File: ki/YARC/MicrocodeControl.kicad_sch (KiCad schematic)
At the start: 24 parts, among them U31 74LS32, U44 74LS574, U45 74LS574, U46 74LS157, U47 74LS157, U48 74LS193, U49 74LS193, U50 74LS139, U51 74LS32, U52 74LS32, U53 74LS157, U54 74LS32

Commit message: Cleanups on the way to first execution - no significant functional changes
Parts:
- renumbered U31 to U54, U44 to U55, U45 to U56, U46 to U57, U47 to U58, U48 to U59, U49 to U60, U50 to U61, U51 to U62, U52 to U63, U53 to U64, U54 to U65
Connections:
- net ~{UC_RAM_OE}: no longer names the net of U60.6 (QC)

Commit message: Add delay line for general register write signal. Minor corrections and cleanups.
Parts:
- renumbered U54 to U31, U55 to U44, U56 to U45, U57 to U46, U58 to U47, U59 to U48, U60 to U49, U61 to U50, U62 to U51, U63 to U52, U64 to U53, U65 to U54

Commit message: Convert schematic to KiCad 7
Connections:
- net GND: now also U54.7 (GND)
- net KCLK0: now also U52.6, U54.11, U54.8; no longer U52.3, U54.3, U54.3
- net SYSCLK: now also U51.4, U51.9, U52.12, U52.4, U54.12, U54.9; no longer U51.1, U51.1, U52.1, U52.1, U54.1, U54.1
- net VCC: now also U54.14 (VCC)
- net ~{KI0EN}: now also U52.10; no longer U52.2
- net ~{KI1EN}: now also U51.13, U51.6; no longer U51.2, U51.3
- net ~{KI2EN}: now also U31.4, U51.8; no longer U31.1, U51.3
- net ~{KI3EN}: now also U52.11; no longer U52.3
- net ~{UC_WE0}: now also U52.8; no longer U52.3
- net ~{UC_WE1}: now also U51.11; no longer U51.3
- net ~{UC_WE2}: now also U31.6; no longer U31.3
- net at U53.9 (Zc): now also U54.10; no longer U54.2
- net at U50.7 (~{Q3}): now also U52.13; no longer U52.2
- net at U53.12 (Zd): now also U54.13; no longer U54.2
- net at U53.11 (I0c): now also U50.10 (~{Q2}); no longer U50.6 (~{Q2})
- net at U53.14 (I0d): now also U50.9 (~{Q3}); no longer U50.7 (~{Q3})
- net at U53.2 (I0a): now also U50.12 (~{Q0}); no longer U50.4 (~{Q0})
- net at U53.5 (I0b): now also U50.11 (~{Q1}); no longer U50.5 (~{Q1})
- net at U53.7 (Zb): now also U52.5; no longer U52.2
- net at U45.13 (Q6): now also U50.15 (~{EN}); no longer U50.1 (~{EN})
- net at U45.14 (Q5): now also U50.13 (B); no longer U50.3 (B)
- net at U45.15 (Q4): now also U50.14 (A); no longer U50.2 (A)
- net at U50.6 (~{Q2}): now also U51.10; no longer U51.2
- net at U50.5 (~{Q1}): now also U51.5; no longer U51.2
- new net: U31.5, U45.16 (Q3), U51.12, U51.2, U52.9

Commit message: Removed about 2/3 of 2300+ errors from the ERC
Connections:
- net KCLK0: no longer U52.6, U54.11, U54.8
- new net KCLK1: U52.6
- new net KCLK2: U54.8
- new net KCLK3: U54.11

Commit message: Ongoing fixes for ERC errors
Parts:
- removed U44: 74LS574, symbol 74xx:74LS574
- renumbered U31 to U54, U45 to U56, U46 to U57, U47 to U58, U48 to U59, U49 to U60, U50 to U61, U51 to U62, U52 to U63, U53 to U64, U54 to U65
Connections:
- net GND: now also U60.14 (CLR), U62.7 (GND), U63.7 (GND)
- net VCC: now also U62.14 (VCC), U63.14 (VCC)
- no-connect marks 0 -> 6
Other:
- note removed: "ALSO ON SHT 8"
- note removed: "IR HIGH (IRH)"

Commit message: Continuing cleanup of schematic
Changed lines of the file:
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@@
     (stroke (width 0) (type default))
   )
-  (bus (pts (xy 60.96 152.4) (xy 60.96 161.29))
+  (bus (pts (xy 60.96 134.62) (xy 60.96 161.29))
     (stroke (width 0) (type default))
   )
@@
     (stroke (width 0) (type default))
   )
-  (bus (pts (xy 60.96 144.78) (xy 60.96 147.32))
-    (stroke (width 0) (type default))
-  )
   (wire (pts (xy 137.16 166.37) (xy 137.16 163.83))
     (stroke (width 0) (type default))
@@
     (stroke (width 0) (type default))
   )
-  (bus (pts (xy 60.96 142.24) (xy 60.96 144.78))
-    (stroke (width 0) (type default))
-  )
   (wire (pts (xy 137.16 105.41) (xy 137.16 107.95))
     (stroke (width 0) (type default))
@@
     (stroke (width 0) (type default))
   )
-  (bus (pts (xy 60.96 139.7) (xy 60.96 142.24))
-    (stroke (width 0) (type default))
-  )
   (wire (pts (xy 105.41 161.29) (xy 111.76 161.29))
     (stroke (width 0) (type default))
@@
     (stroke (width 0) (type default))
   )
-  (bus (pts (xy 60.96 134.62) (xy 60.96 137.16))
-    (stroke (width 0) (type default))
-  )
   (wire (pts (xy 228.6 24.13) (xy 245.11 24.13))
     (stroke (width 0) (type default))
@@
     (stroke (width 0) (type default))
   )
-  (bus (pts (xy 60.96 147.32) (xy 60.96 149.86))
-    (stroke (width 0) (type default))
-  )
   (wire (pts (xy 166.37 57.15) (xy 173.99 57.15))
     (stroke (width 0) (type default))
@@
     (stroke (width 0) (type default))
   )
-  (bus (pts (xy 60.96 149.86) (xy 60.96 152.4))
-    (stroke (width 0) (type default))
-  )
   (wire (pts (xy 55.88 45.72) (xy 111.76 45.72))
     (stroke (width 0) (type default))
@@
     (stroke (width 0) (type default))
   )
-  (bus (pts (xy 60.96 137.16) (xy 60.96 139.7))
-    (stroke (width 0) (type default))
-  )

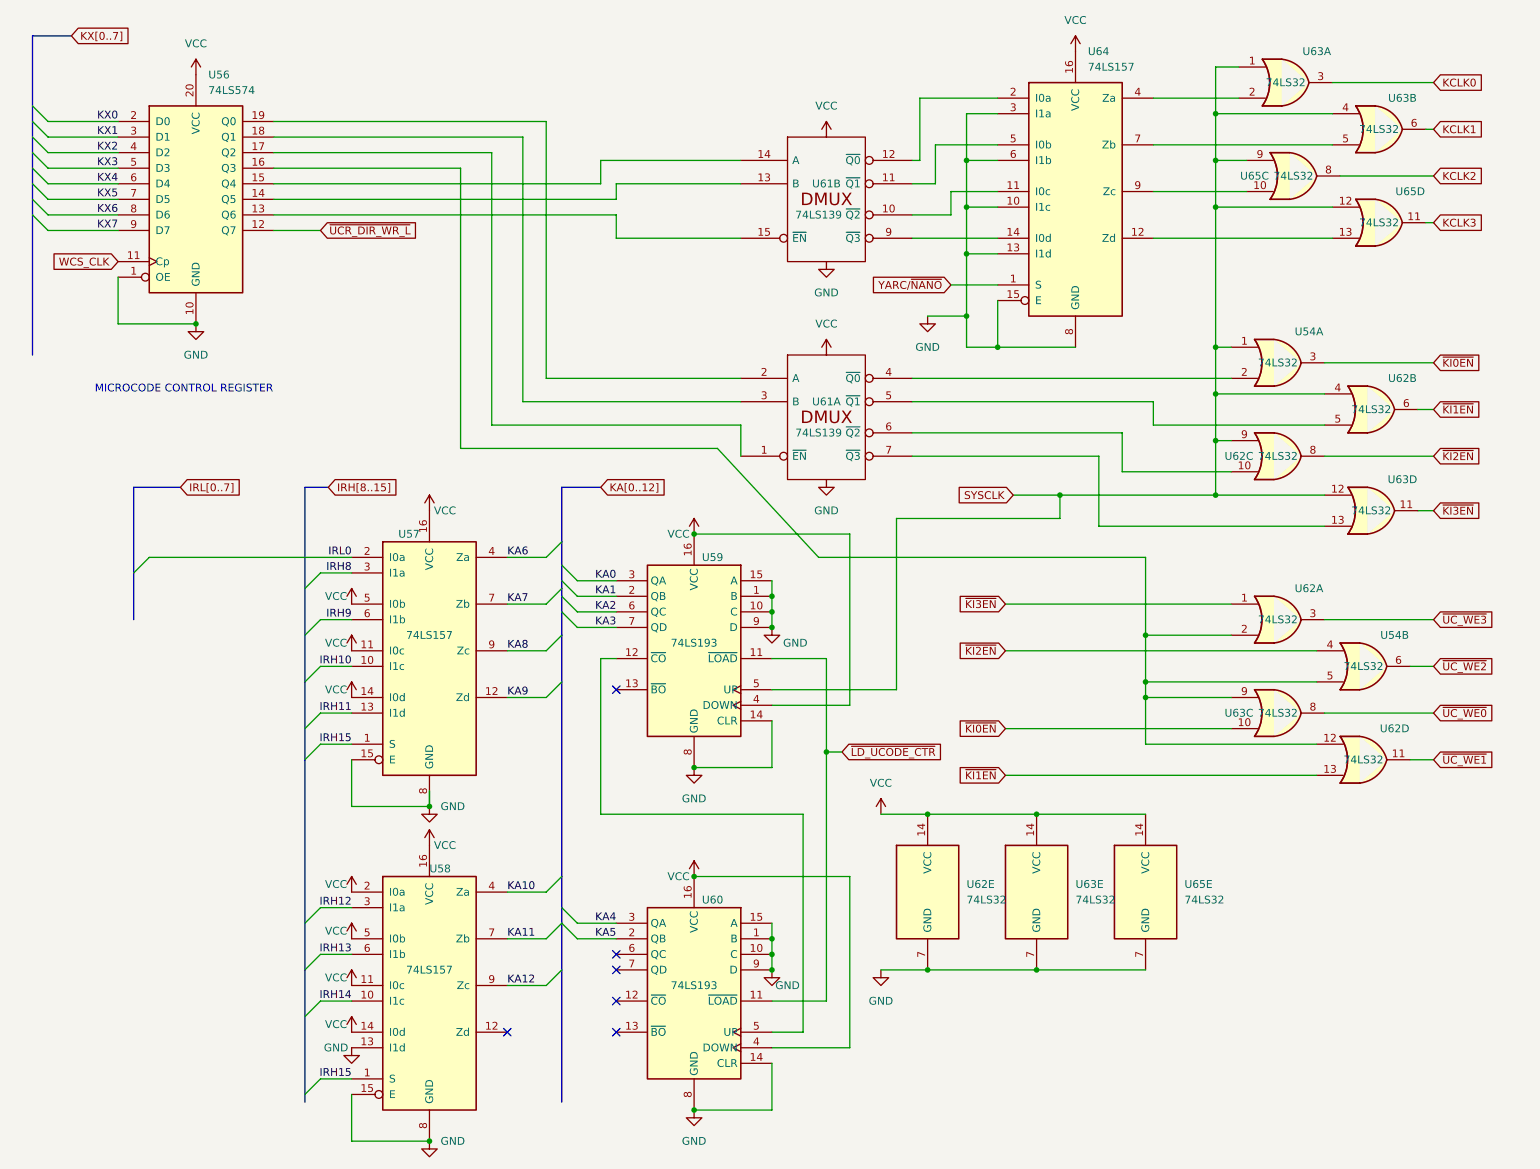
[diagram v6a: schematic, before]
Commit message: Schematic for addressing unit is complete and all ERC violations addressed
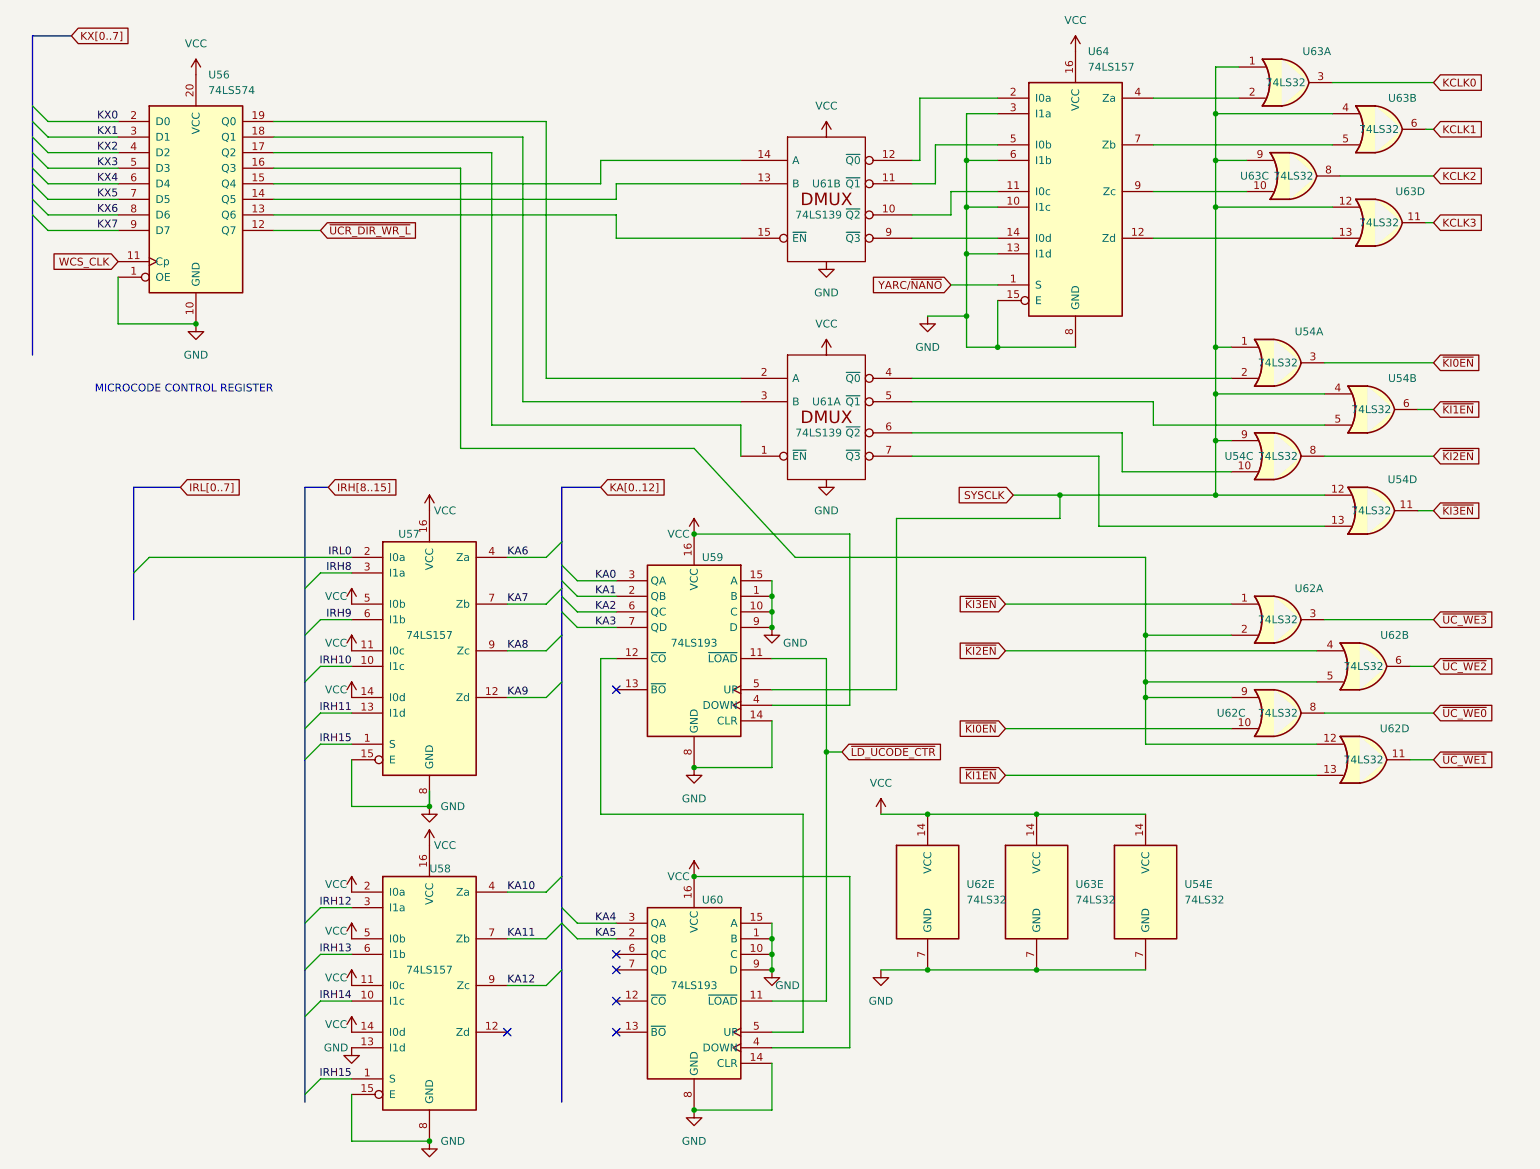
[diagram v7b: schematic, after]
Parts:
- renumbered U63 to U54, U62 to U54, U65 to U54, U54 to U62, U63 to U62, U65 to U63
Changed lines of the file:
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@@
     (stroke (width 0) (type default))
   )
-  (wire (pts (xy 86.36 83.82) (xy 128.27 83.82))
+  (wire (pts (xy 86.36 83.82) (xy 124.46 83.82))
     (stroke (width 0) (type default))
   )
@@
     (stroke (width 0) (type default))
   )
-  (wire (pts (xy 144.78 101.6) (xy 198.12 101.6))
+  (wire (pts (xy 140.97 101.6) (xy 198.12 101.6))
     (stroke (width 0) (type default))
   )
@@
     (stroke (width 0) (type default))
   )
-  (wire (pts (xy 128.27 83.82) (xy 144.78 101.6))
+  (wire (pts (xy 124.46 83.82) (xy 140.97 101.6))
     (stroke (width 0) (type default))
   )
@@
   (symbol (lib_id "74xx:74LS32") (at 222.25 39.37 0) (unit 3)
     (in_bom yes) (on_board yes) (dnp no)
-    (property "Reference" "U65" (at 215.9 39.37 0)
+    (property "Reference" "U63" (at 215.9 39.37 0)
       (effects (font (size 1.27 1.27)))
     )
@@
       (project "YARC"
         (path "/22e0f8e1-b0d7-4d47-bb7c-8ef04cd95fca/a3892bed-2422-46c3-a2f7-c55c7ea6ac93"
-          (reference "U65") (unit 3)
+          (reference "U63") (unit 3)
         )
       )
@@
   (symbol (lib_id "74xx:74LS32") (at 234.95 93.98 0) (unit 4)
     (in_bom yes) (on_board yes) (dnp no)
-    (property "Reference" "U63" (at 240.03 88.9 0)
+    (property "Reference" "U54" (at 240.03 88.9 0)
       (effects (font (size 1.27 1.27)))
     )
@@
       (project "YARC"
         (path "/22e0f8e1-b0d7-4d47-bb7c-8ef04cd95fca/a3892bed-2422-46c3-a2f7-c55c7ea6ac93"
-          (reference "U63") (unit 4)
+          (reference "U54") (unit 4)
         )
       )
@@
   (symbol (lib_id "74xx:74LS32") (at 236.22 46.99 0) (unit 4)
     (in_bom yes) (on_board yes) (dnp no)
-    (property "Reference" "U65" (at 241.3 41.91 0)
+    (property "Reference" "U63" (at 241.3 41.91 0)
       (effects (font (size 1.27 1.27)))
     )
@@
       (project "YARC"
         (path "/22e0f8e1-b0d7-4d47-bb7c-8ef04cd95fca/a3892bed-2422-46c3-a2f7-c55c7ea6ac93"
-          (reference "U65") (unit 4)
+          (reference "U63") (unit 4)
         )
       )
@@
   (symbol (lib_id "74xx:74LS32") (at 233.68 119.38 0) (unit 2)
     (in_bom yes) (on_board yes) (dnp no)
-    (property "Reference" "U54" (at 238.76 114.3 0)
+    (property "Reference" "U62" (at 238.76 114.3 0)
       (effects (font (size 1.27 1.27)))
     )
@@
       (project "YARC"
         (path "/22e0f8e1-b0d7-4d47-bb7c-8ef04cd95fca/a3892bed-2422-46c3-a2f7-c55c7ea6ac93"
-          (reference "U54") (unit 2)
+          (reference "U62") (unit 2)
         )
       )
@@
   (symbol (lib_id "74xx:74LS32") (at 219.71 85.09 0) (unit 3)
     (in_bom yes) (on_board yes) (dnp no)
-    (property "Reference" "U62" (at 213.36 85.09 0)
+    (property "Reference" "U54" (at 213.36 85.09 0)
       (effects (font (size 1.27 1.27)))
     )
@@
       (project "YARC"
         (path "/22e0f8e1-b0d7-4d47-bb7c-8ef04cd95fca/a3892bed-2422-46c3-a2f7-c55c7ea6ac93"
-          (reference "U62") (unit 3)
+          (reference "U54") (unit 3)
         )
       )
@@
   (symbol (lib_id "74xx:74LS32") (at 219.71 127 0) (unit 3)
     (in_bom yes) (on_board yes) (dnp no)
-    (property "Reference" "U63" (at 213.36 127 0)
+    (property "Reference" "U62" (at 212.09 127 0)
       (effects (font (size 1.27 1.27)))
     )
@@
       (project "YARC"
         (path "/22e0f8e1-b0d7-4d47-bb7c-8ef04cd95fca/a3892bed-2422-46c3-a2f7-c55c7ea6ac93"
-          (reference "U63") (unit 3)
+          (reference "U62") (unit 3)
         )
       )
@@
   (symbol (lib_id "74xx:74LS32") (at 234.95 77.47 0) (unit 2)
     (in_bom yes) (on_board yes) (dnp no)
-    (property "Reference" "U62" (at 240.03 72.39 0)
+    (property "Reference" "U54" (at 240.03 72.39 0)
       (effects (font (size 1.27 1.27)))
     )
@@
       (project "YARC"
         (path "/22e0f8e1-b0d7-4d47-bb7c-8ef04cd95fca/a3892bed-2422-46c3-a2f7-c55c7ea6ac93"
-          (reference "U62") (unit 2)
+          (reference "U54") (unit 2)
         )
       )
@@
   (symbol (lib_id "74xx:74LS32") (at 198.12 156.21 0) (unit 5)
     (in_bom yes) (on_board yes) (dnp no) (fields_autoplaced)
-    (property "Reference" "U65" (at 204.47 154.9399 0)
+    (property "Reference" "U54" (at 204.47 154.9399 0)
       (effects (font (size 1.27 1.27)) (justify left))
     )
@@
       (project "YARC"
         (path "/22e0f8e1-b0d7-4d47-bb7c-8ef04cd95fca/a3892bed-2422-46c3-a2f7-c55c7ea6ac93"
-          (reference "U65") (unit 5)
-        )
-      )
+          (reference "U54") (unit 5)
+        )
+      )
